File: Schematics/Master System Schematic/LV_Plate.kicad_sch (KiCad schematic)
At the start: 3 parts, among them U10 OrionBMS2, U8 Bender_Isometer_IR155-3204, U9 OrionThermExp

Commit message: LV Plate update
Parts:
- removed U10: OrionBMS2, symbol NER:OrionBMS2
- removed U8: Bender_Isometer_IR155-3204, symbol NER:Bender_Isometer_IR155-3204
- removed U9: OrionThermExp, symbol NER:OrionThermExp
- added U?: Shep_Controller, symbol NER:Shep_Controller
- added U?: Bender_Isometer_IR155-3204, symbol NER:Bender_Isometer_IR155-3204
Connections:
- net BMS_Fault: now also U?.12 (Fault_Rly)
- net BattFanPWM: now also U?.6 (GND)
- net CHRG_DETECT1: now also U?.10 (GND)
- net CHRG_DETECT2: now also U?.22 (Digital4)
- net CHRG_GND: now also U?.11 (GND)
- net CHRG_SAFETY: now also U?.21 (Digital3)
- net GLV_Chassis1: now also U?.~ (STATUS_OK)
- net GLV_Chassis2: now also U?.~ (STATUS_OK)
- net GND: now also U?.2 (isoSPI_P), U?.~ (STATUS_OK)
- net HV_Sense+: now also U?.~ (STATUS_OK)
- net HV_Sense-: now also U?.~ (STATUS_OK)
- net IMD_Fault: now also U?.~ (STATUS_OK)
- net LVPlate_GLV+: now also U?.1 (Shield), U?.~ (STATUS_OK)
- new net: U?.11 (GND), U?.4 (isoSPI_M)
- no-connect marks 27 -> 1
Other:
- removed sheet MCR_PCB
- note added: "From HV Plate below"
- note added: "To HV Plate area"
- note added: "To HV Plate control connector"
- note removed: "13x 22AWG"
- note removed: "16x 22AWG"
- note removed: "22AWG"
- note removed: "24x 22AWG"
- note removed: "GLV Conn Cutout"
- note removed: "HV Cutout - from HV Plate below"
- note removed: "Indicator Cutout - in Accum. Wall"
- note removed: "Therm Cutout"
- note removed: "VT Cutout"
- title: LV_Plate -> LV Plate

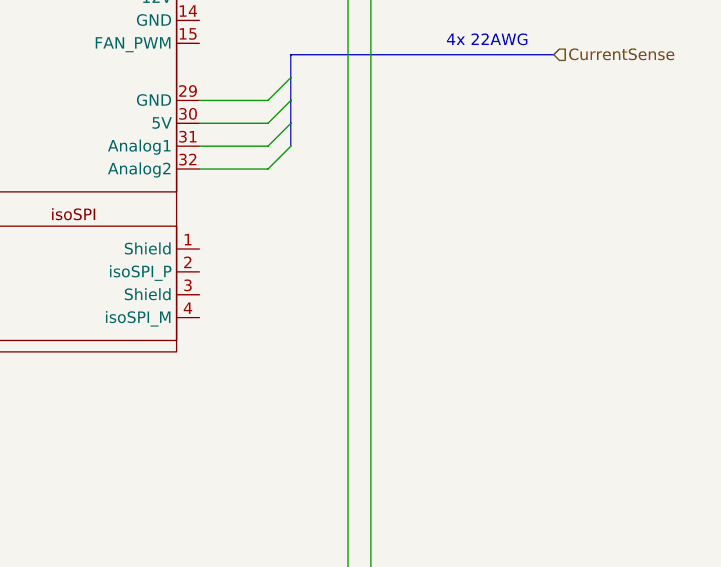
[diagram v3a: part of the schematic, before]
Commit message: Partial work on accumulator container sheet
To be continued
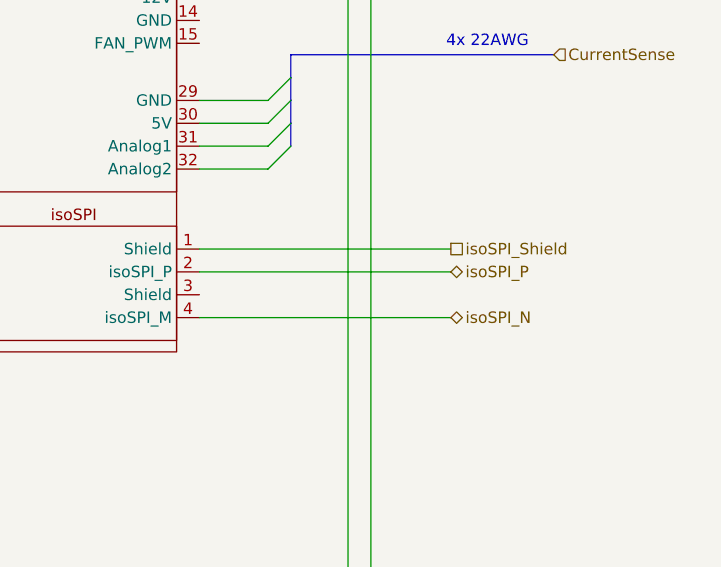
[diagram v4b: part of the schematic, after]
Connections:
- net isoSPI_Shield: now reaches U?.1 (Shield)
- net isoSPI_N: now reaches U?.4 (isoSPI_M)
- net isoSPI_N: no longer U?.11 (GND)
- net isoSPI_P: now reaches U?.2 (isoSPI_P)
- new net: U?.11 (GND), U?.4 (isoSPI_M)
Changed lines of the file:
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@@
+    (stroke (width 0) (type default) (color 0 0 0 0))
+  )
+  (wire (pts (xy 313.69 158.75) (xy 341.63 158.75))
     (stroke (width 0) (type default) (color 0 0 0 0))
   )
@@
     (stroke (width 0) (type default) (color 0 0 0 0))
   )
+  (wire (pts (xy 313.69 156.21) (xy 341.63 156.21))
+    (stroke (width 0) (type default) (color 0 0 0 0))
+  )
   (wire (pts (xy 217.17 186.69) (xy 231.14 186.69))
     (stroke (width 0) (type default) (color 0 0 0 0))
@@
   )
   (wire (pts (xy 254 148.59) (xy 265.43 148.59))
+    (stroke (width 0) (type default) (color 0 0 0 0))
+  )
+  (wire (pts (xy 313.69 163.83) (xy 341.63 163.83))
     (stroke (width 0) (type default) (color 0 0 0 0))
   )
@@
     (effects (font (size 1.27 1.27)) (justify left bottom))
   )
+  (hierarchical_label "isoSPI_P" (shape bidirectional) (at 341.63 158.75 0)
+    (effects (font (size 1.27 1.27)) (justify left))
+  )
   (hierarchical_label "GLV_CANH" (shape input) (at 214.63 100.33 180)
     (effects (font (size 1.27 1.27)) (justify right))
@@
     (effects (font (size 1.27 1.27)) (justify right))
   )
+  (hierarchical_label "isoSPI_N" (shape bidirectional) (at 341.63 163.83 0)
+    (effects (font (size 1.27 1.27)) (justify left))
+  )
   (hierarchical_label "MC_Precharge+" (shape input) (at 200.66 148.59 0)
     (effects (font (size 1.27 1.27)) (justify left))
@@
     (effects (font (size 1.27 1.27)) (justify left))
   )
+  (hierarchical_label "isoSPI_Shield" (shape passive) (at 341.63 156.21 0)
+    (effects (font (size 1.27 1.27)) (justify left))
+  )

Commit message: Finish accumulator
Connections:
- net DCDC PCB/CurrentMeas: now reaches U?.15 (FAN_PWM)
- net DCDC PCB/VoltageMeas: now reaches U?.16 (Analog4)
- net DCDC PCB/Sig_GND: now reaches U?.18 (GND)
- net DCDC PCB/PGOOD: now reaches U?.19 (Digital5)
- new net: U?.11 (GND), U?.4 (isoSPI_M)
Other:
- added sheet DCDC PCB (DCDC.kicad_sch)
- sheet TSAL PCB ports: added TSAL_ACTIVE, TSAL_GND; removed TSALGND, TSAL_30V

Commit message: Renumbered pages
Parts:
- gave numbers to parts that had none: 2
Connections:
- new net: U1202.11 (GND), U1202.4 (isoSPI_M)
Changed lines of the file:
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@@
   (symbol (lib_id "NER:Shep_Controller") (at 289.56 91.44 0) (unit 1)
     (in_bom yes) (on_board yes) (fields_autoplaced)
-    (property "Reference" "U?" (id 0) (at 289.56 87.63 0))
+    (property "Reference" "U1202" (id 0) (at 289.56 87.63 0))
     (property "Value" "Shep_Controller" (id 1) (at 289.56 90.17 0))
     (property "Footprint" "" (id 2) (at 289.56 86.36 0)
@@
   (symbol (lib_id "NER:Bender_Isometer_IR155-3204") (at 152.4 110.49 0) (unit 1)
     (in_bom yes) (on_board yes)
-    (property "Reference" "U?" (id 0) (at 152.4 107.569 0))
+    (property "Reference" "U1201" (id 0) (at 152.4 107.569 0))
     (property "Value" "Bender_Isometer_IR155-3204" (id 1) (at 152.4 109.8804 0))
     (property "Footprint" "" (id 2) (at 152.4 110.49 0)

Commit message: Annotations
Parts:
- renumbered U1201 to U601, U1202 to U602
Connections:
- new net: U602.11 (GND), U602.4 (isoSPI_M)
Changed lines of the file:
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@@
   (symbol (lib_id "NER:Shep_Controller") (at 289.56 91.44 0) (unit 1)
     (in_bom yes) (on_board yes) (fields_autoplaced)
-    (property "Reference" "U1202" (id 0) (at 289.56 87.63 0))
+    (property "Reference" "U602" (id 0) (at 289.56 87.63 0))
     (property "Value" "Shep_Controller" (id 1) (at 289.56 90.17 0))
     (property "Footprint" "" (id 2) (at 289.56 86.36 0)
@@
   (symbol (lib_id "NER:Bender_Isometer_IR155-3204") (at 152.4 110.49 0) (unit 1)
     (in_bom yes) (on_board yes)
-    (property "Reference" "U1201" (id 0) (at 152.4 107.569 0))
+    (property "Reference" "U601" (id 0) (at 152.4 107.569 0))
     (property "Value" "Bender_Isometer_IR155-3204" (id 1) (at 152.4 109.8804 0))
     (property "Footprint" "" (id 2) (at 152.4 110.49 0)

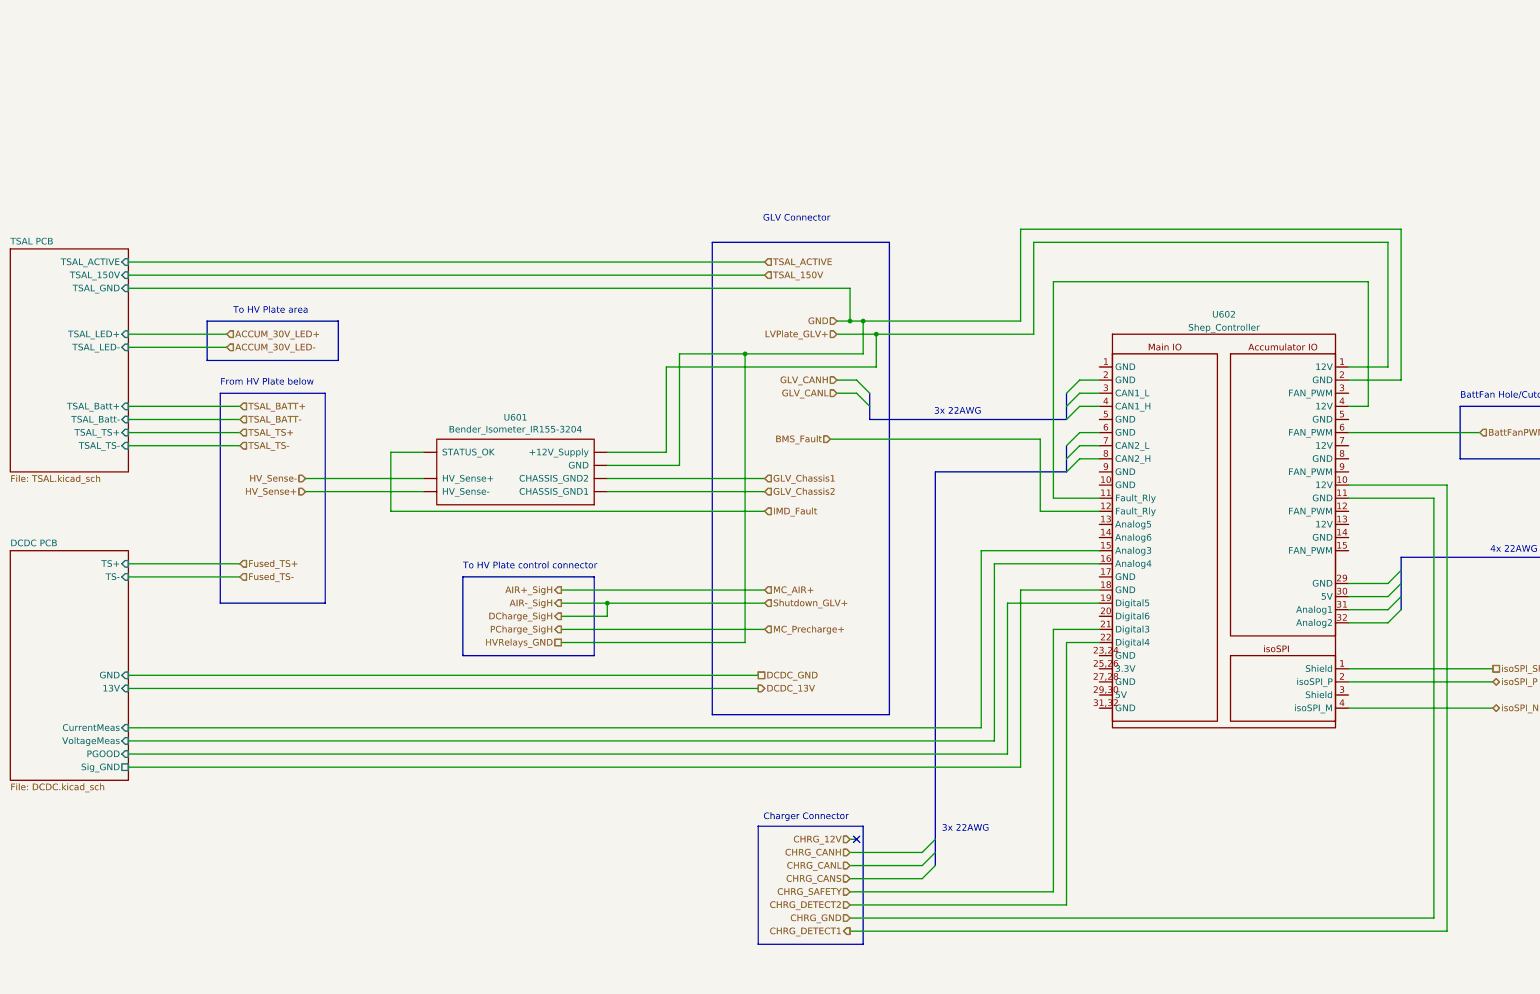
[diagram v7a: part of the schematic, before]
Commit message: More annotate and export
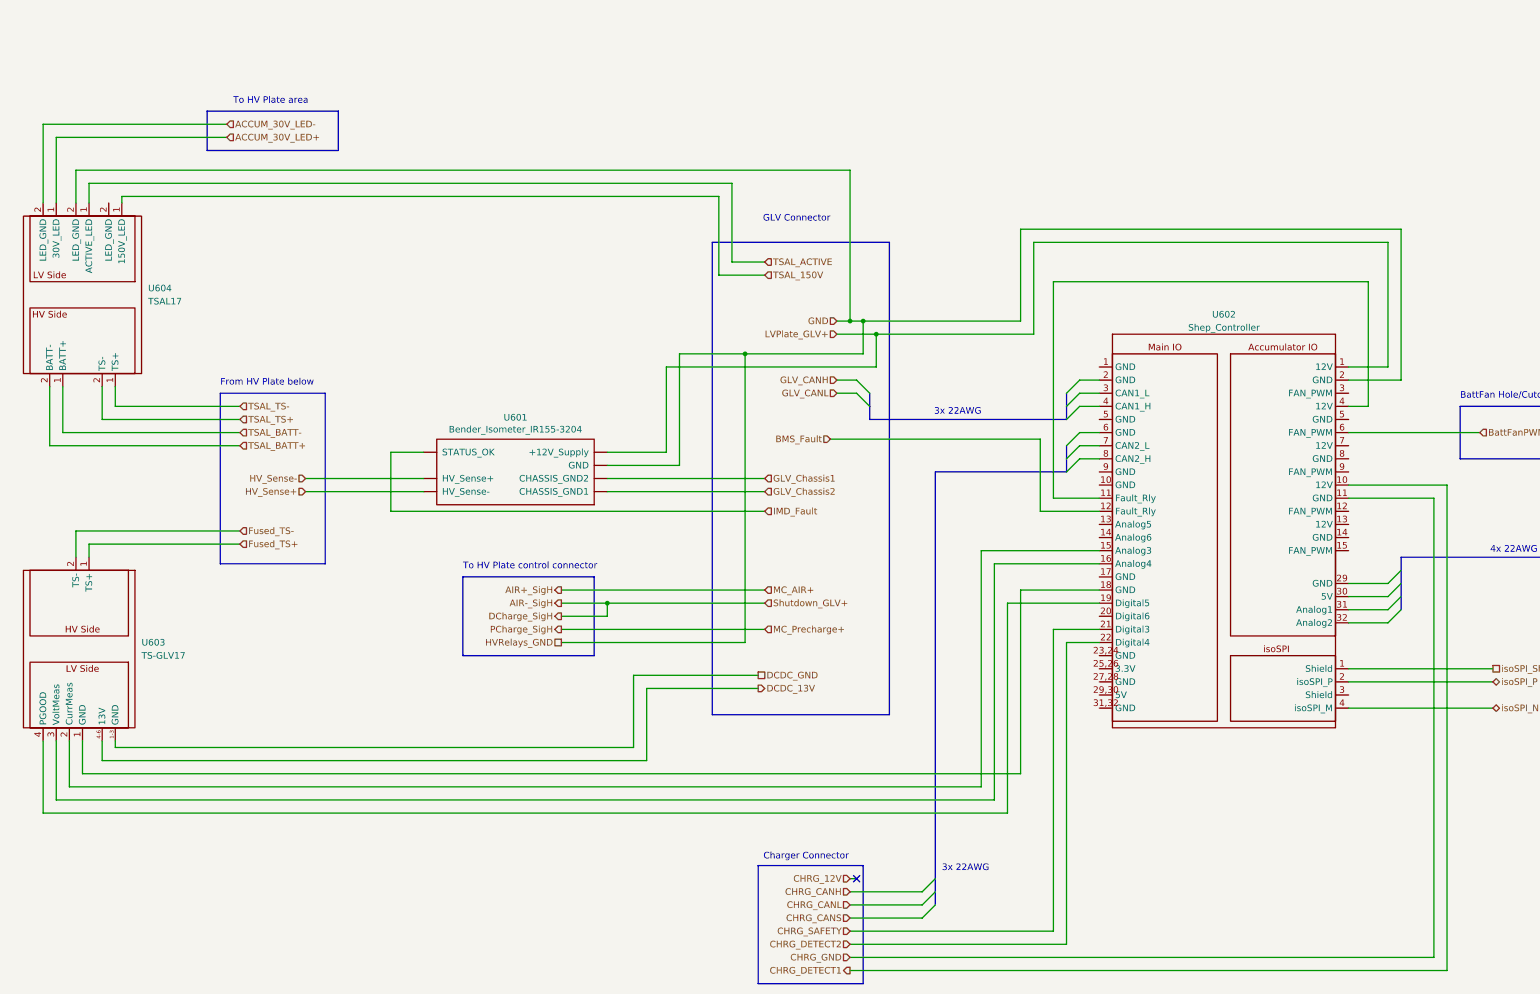
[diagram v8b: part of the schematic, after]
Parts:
- added U603: TS-GLV17, symbol NER:TS-GLV17
- added U604: TSAL17, symbol NER:TSAL17
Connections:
- net DCDC PCB/CurrentMeas is gone; now on an unnamed net: U602.15 (FAN_PWM)
- net ACCUM_30V_LED+: now also U604.1 (TS+)
- net ACCUM_30V_LED-: now also U604.2 (TS-)
- net DCDC_13V: now also U603.4-6 (13V)
- net DCDC_GND: now also U603.1-3 (GND)
- net Fused_TS+: now also U603.1 (TS+)
- net Fused_TS-: now also U603.2 (TS-)
- net GND: now also U604.2 (TS-)
- net TSAL_150V: now also U604.1 (TS+)
- net TSAL_ACTIVE: now also U604.1 (TS+)
- net TSAL_BATT+: now also U604.2 (TS-)
- net TSAL_BATT-: now also U604.1 (TS+)
- net TSAL_TS+: now also U604.2 (TS-)
- net TSAL_TS-: now also U604.1 (TS+)
- net at U602.15 (FAN_PWM): now also U603.2 (TS-)
- net DCDC PCB/PGOOD: no longer names the net of U602.19 (Digital5)
- net DCDC PCB/PGOOD: now also U603.4 (PGOOD)
- net DCDC PCB/Sig_GND: no longer names the net of U602.18 (GND)
- net DCDC PCB/Sig_GND: now also U603.1 (TS+)
- net DCDC PCB/VoltageMeas: no longer names the net of U602.16 (Analog4)
- net DCDC PCB/VoltageMeas: now also U603.3 (VoltMeas)
- new net: U602.11 (GND), U602.4 (isoSPI_M)
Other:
- removed sheet DCDC PCB
- removed sheet TSAL PCB
